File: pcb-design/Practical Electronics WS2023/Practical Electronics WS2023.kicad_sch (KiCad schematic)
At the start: 38 parts, among them IC1 SN74LVC2G04DBVT, J1 PWR Jack, J2 MIDI Input, J3 MIDI Thru out, J4 Conn_01x03, J5 ISP, Q1 Q_NMOS_DGS, SW1 SW_SPDT, SW2 SW_SPDT, SW4 SW_SPDT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

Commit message: removed led detector
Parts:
- removed Q1: Q_NMOS_DGS, symbol Device:Q_NMOS_DGS
- removed R8: 10k, symbol Device:R
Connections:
- net LED GND is gone; now on net GND: J4.1 (Pin_1)
- no-connect marks 22 -> 23
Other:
- note removed: "LED strip detector"
- note removed: "When LED is connected - PIN3 is LOW. Internal pull-up resistor should be used."
- moved on the sheet: J4

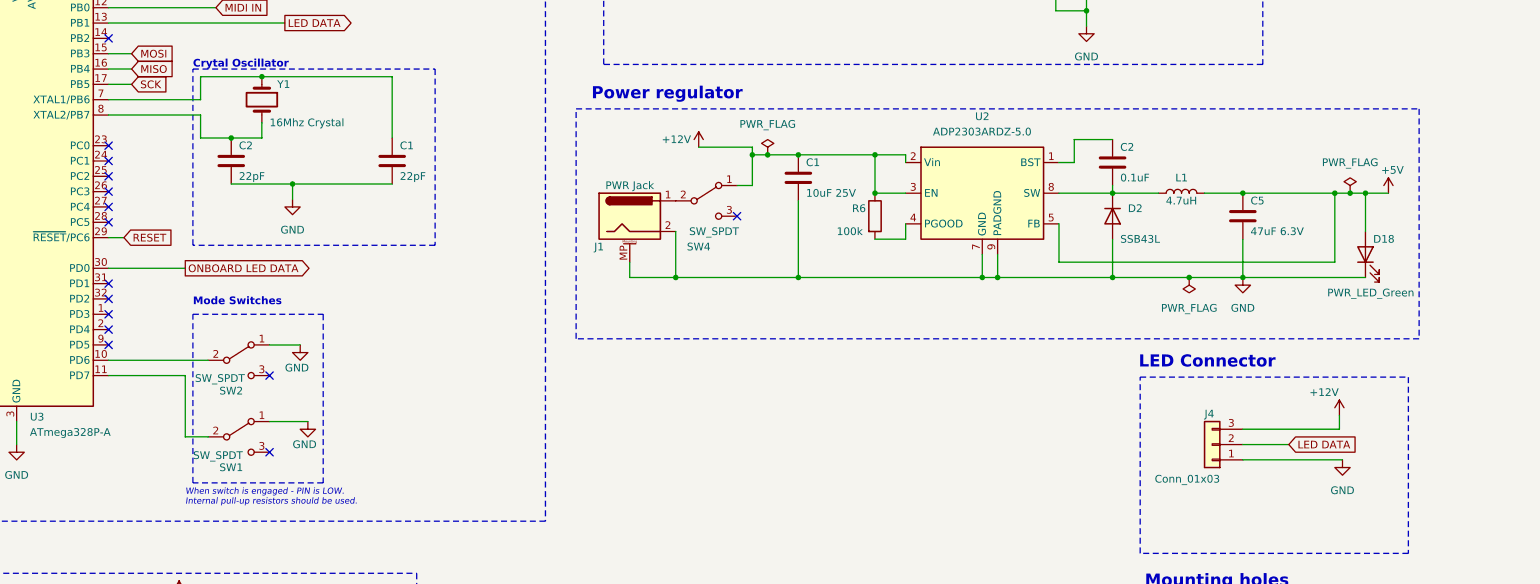
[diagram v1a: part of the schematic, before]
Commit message: replaced sitches with switch connectors
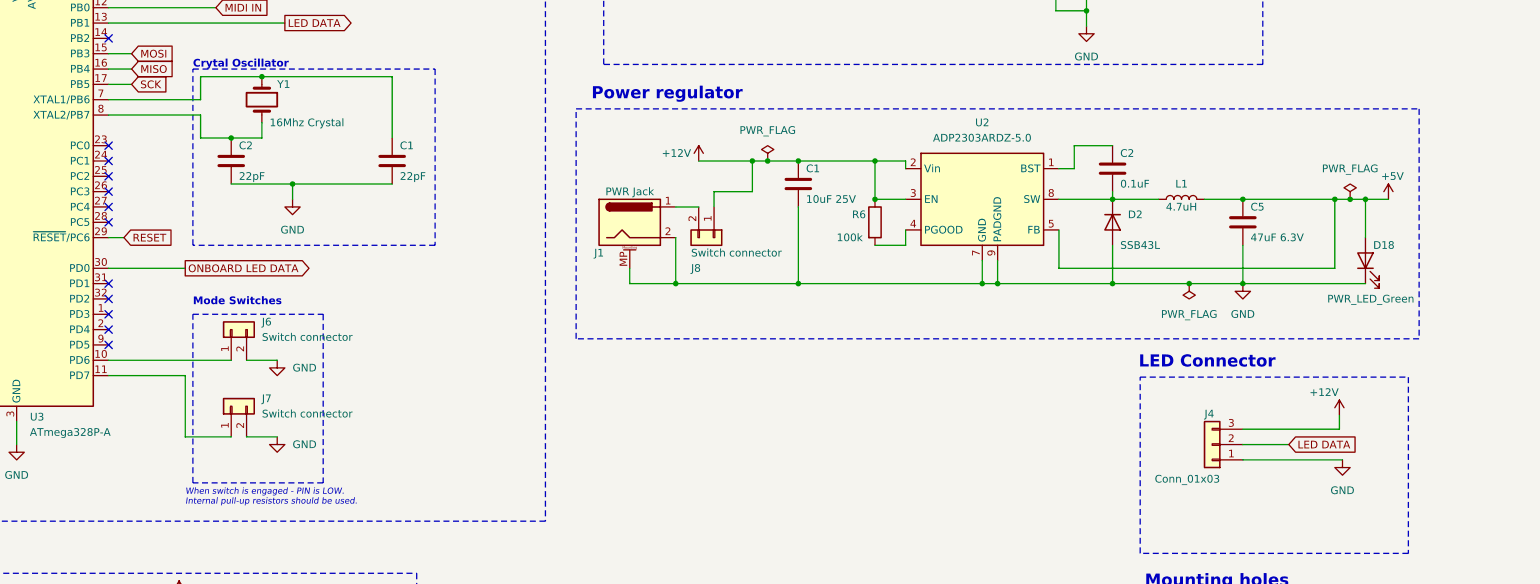
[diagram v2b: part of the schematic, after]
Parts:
- removed SW1, SW2, SW4: SW_SPDT, symbol Switch:SW_SPDT
- added J6, J7, J8: Switch connector, symbol Connector_Generic:Conn_01x02
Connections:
- net +12V: now also J8.1 (Pin_1)
- net GND: now also J6.2 (Pin_2), J7.2 (Pin_2)
- net at U3.10 (PD6): now also J6.1 (Pin_1)
- net at J1.1: now also J8.2 (Pin_2)
- net at U3.11 (PD7): now also J7.1 (Pin_1)
- no-connect marks 23 -> 20
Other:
- moved on the sheet: C1, C2, C5, D18, D2, J1, L1, R6, U2

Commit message: most of the footprints assigned
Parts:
- C1: footprint (none) -> Capacitor_SMD:C_Elec_4x5.4
- C1, C2, C5: footprint (none) -> Capacitor_SMD:C_1206_3216Metric_Pad1.33x1.80mm_HandSolder
- D18: footprint (none) -> LED_SMD:LED_1206_3216Metric
- H1, H2, H3, H4: footprint (none) -> MountingHole:MountingHole_3mm
- J1: footprint (none) -> Connector_BarrelJack:BarrelJack_Horizontal
- J4: footprint (none) -> Connector_JST:JST_PH_B3B-PH-K_1x03_P2.00mm_Vertical
- J5: footprint (none) -> Connector_PinHeader_2.00mm:PinHeader_2x03_P2.00mm_Vertical
- J6, J7, J8: footprint (none) -> Connector_JST:JST_PH_B2B-PH-K_1x02_P2.00mm_Vertical
- L1, R2, R3, R4, R5, R6, R7: footprint (none) -> Resistor_SMD:R_1206_3216Metric_Pad1.30x1.75mm_HandSolder
- U1: footprint (none) -> Package_DIP:SMDIP-8_W9.53mm
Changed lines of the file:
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@@
       (effects (font (size 1.27 1.27)))
     )
-    (property "Footprint" "" (at 85.344 145.034 90)
+    (property "Footprint" "Resistor_SMD:R_1206_3216Metric_Pad1.30x1.75mm_HandSolder" (at 85.344 145.034 90)
       (effects (font (size 1.27 1.27)) hide)
     )
@@
       (effects (font (size 1.27 1.27)) (justify left))
     )
-    (property "Footprint" "" (at 180.0352 76.2 0)
+    (property "Footprint" "Capacitor_SMD:C_Elec_4x5.4" (at 180.0352 76.2 0)
       (effects (font (size 1.27 1.27)) hide)
     )
@@
       (effects (font (size 1.27 1.27)) (justify left))
     )
-    (property "Footprint" "" (at 231.902 28.448 0)
+    (property "Footprint" "Resistor_SMD:R_1206_3216Metric_Pad1.30x1.75mm_HandSolder" (at 231.902 28.448 0)
       (effects (font (size 1.27 1.27)) hide)
     )
@@
       (effects (font (size 1.27 1.27)))
     )
-    (property "Footprint" "" (at 218.948 37.338 0)
+    (property "Footprint" "Package_DIP:SMDIP-8_W9.53mm" (at 218.948 37.338 0)
       (effects (font (size 1.27 1.27)) hide)
     )
@@
       (effects (font (size 1.27 1.27)))
     )
-    (property "Footprint" "" (at 150.368 185.801 0)
+    (property "Footprint" "Connector_PinHeader_2.00mm:PinHeader_2x03_P2.00mm_Vertical" (at 150.368 185.801 0)
       (effects (font (size 1.27 1.27)) hide)
     )
@@
       (effects (font (size 1.27 1.27)) (justify left))
     )
-    (property "Footprint" "" (at 226.822 38.608 0)
+    (property "Footprint" "Resistor_SMD:R_1206_3216Metric_Pad1.30x1.75mm_HandSolder" (at 226.822 38.608 0)
       (effects (font (size 1.27 1.27)) hide)
     )
@@
       (effects (font (size 1.27 1.27)) (justify left))
     )
-    (property "Footprint" "" (at 189.992 78.74 90)
+    (property "Footprint" "Resistor_SMD:R_1206_3216Metric_Pad1.30x1.75mm_HandSolder" (at 189.992 78.74 90)
       (effects (font (size 1.27 1.27)) hide)
     )
@@
       (effects (font (size 1.27 1.27)) (justify left))
     )
-    (property "Footprint" "" (at 262.128 145.669 0)
+    (property "Footprint" "MountingHole:MountingHole_3mm" (at 262.128 145.669 0)
       (effects (font (size 1.27 1.27)) hide)
     )
@@
       (effects (font (size 1.27 1.27)) (justify right))
     )
-    (property "Footprint" "" (at 75.4888 161.036 0)
+    (property "Footprint" "Capacitor_SMD:C_1206_3216Metric_Pad1.33x1.80mm_HandSolder" (at 75.4888 161.036 0)
       (effects (font (size 1.27 1.27)) hide)
     )
@@
       (effects (font (size 1.27 1.27)) (justify left))
     )
-    (property "Footprint" "" (at 240.919 156.718 0)
+    (property "Footprint" "MountingHole:MountingHole_3mm" (at 240.919 156.718 0)
       (effects (font (size 1.27 1.27)) hide)
     )
@@
       (effects (font (size 1.27 1.27)))
     )
-    (property "Footprint" "" (at 242.57 74.93 0)
+    (property "Footprint" "Resistor_SMD:R_1206_3216Metric_Pad1.30x1.75mm_HandSolder" (at 242.57 74.93 0)
       (effects (font (size 1.27 1.27)) hide)
     )
@@
       (effects (font (size 1.27 1.27)))
     )
-    (property "Footprint" "" (at 86.614 160.274 90)
+    (property "Footprint" "Resistor_SMD:R_1206_3216Metric_Pad1.30x1.75mm_HandSolder" (at 86.614 160.274 90)
       (effects (font (size 1.27 1.27)) hide)
     )
@@
       (effects (font (size 1.27 1.27)) (justify right))
     )
-    (property "Footprint" "" (at 85.09 96.52 0)
+    (property "Footprint" "Connector_JST:JST_PH_B2B-PH-K_1x02_P2.00mm_Vertical" (at 85.09 96.52 0)
       (effects (font (size 1.27 1.27)) hide)
     )
@@
       (effects (font (size 1.27 1.27)) (justify right))
     )
-    (property "Footprint" "" (at 85.09 109.22 0)
+    (property "Footprint" "Connector_JST:JST_PH_B2B-PH-K_1x02_P2.00mm_Vertical" (at 85.09 109.22 0)
       (effects (font (size 1.27 1.27)) hide)
     )
@@
       (effects (font (size 1.27 1.27)))
     )
-    (property "Footprint" "" (at 152.4 79.756 0)
+    (property "Footprint" "Connector_BarrelJack:BarrelJack_Horizontal" (at 152.4 79.756 0)
       (effects (font (size 1.27 1.27)) hide)
     )
@@
       (effects (font (size 1.27 1.27)) (justify left))
     )
-    (property "Footprint" "" (at 22.3012 33.02 0)
+    (property "Footprint" "Capacitor_SMD:C_1206_3216Metric_Pad1.33x1.80mm_HandSolder" (at 22.3012 33.02 0)
       (effects (font (size 1.27 1.27)) hide)
     )
@@
       (effects (font (size 1.27 1.27)) (justify left))
     )
-    (property "Footprint" "" (at 262.128 157.226 0)
+    (property "Footprint" "MountingHole:MountingHole_3mm" (at 262.128 157.226 0)
       (effects (font (size 1.27 1.27)) hide)
     )
@@
       (effects (font (size 1.27 1.27)) (justify left))
     )
-    (property "Footprint" "" (at 40.5892 33.02 0)
+    (property "Footprint" "Capacitor_SMD:C_1206_3216Metric_Pad1.33x1.80mm_HandSolder" (at 40.5892 33.02 0)
       (effects (font (size 1.27 1.27)) hide)
     )
@@
       (effects (font (size 1.27 1.27)) (justify left))
     )
-    (property "Footprint" "" (at 86.0552 72.39 0)
+    (property "Footprint" "Capacitor_SMD:C_1206_3216Metric_Pad1.33x1.80mm_HandSolder" (at 86.0552 72.39 0)
       (effects (font (size 1.27 1.27)) hide)
     )
@@
       (effects (font (size 1.27 1.27)) (justify left))
     )
-    (property "Footprint" "" (at 253.6952 82.55 0)
+    (property "Footprint" "Capacitor_SMD:C_1206_3216Metric_Pad1.33x1.80mm_HandSolder" (at 253.6952 82.55 0)
       (effects (font (size 1.27 1.27)) hide)
     )
@@
       (effects (font (size 1.27 1.27)) (justify right))
     )
-    (property "Footprint" "" (at 247.65 115.57 0)
+    (property "Footprint" "Connector_JST:JST_PH_B3B-PH-K_1x03_P2.00mm_Vertical" (at 247.65 115.57 0)
       (effects (font (size 1.27 1.27)) hide)
     )
@@
       (effects (font (size 1.27 1.27)) (justify right))
     )
-    (property "Footprint" "" (at 273.05 85.09 0)
+    (property "Footprint" "LED_SMD:LED_1206_3216Metric" (at 273.05 85.09 0)
       (effects (font (size 1.27 1.27)) hide)
     )
@@
       (effects (font (size 1.27 1.27)) (justify left))
     )
-    (property "Footprint" "" (at 241.046 145.542 0)
+    (property "Footprint" "MountingHole:MountingHole_3mm" (at 241.046 145.542 0)
       (effects (font (size 1.27 1.27)) hide)
     )
@@
       (effects (font (size 1.27 1.27)) (justify left))
     )
-    (property "Footprint" "" (at 232.1052 73.66 0)
+    (property "Footprint" "Capacitor_SMD:C_1206_3216Metric_Pad1.33x1.80mm_HandSolder" (at 232.1052 73.66 0)
       (effects (font (size 1.27 1.27)) hide)
     )
@@
       (effects (font (size 1.27 1.27)) (justify left))
     )
-    (property "Footprint" "" (at 31.6992 33.02 0)
+    (property "Footprint" "Capacitor_SMD:C_1206_3216Metric_Pad1.33x1.80mm_HandSolder" (at 31.6992 33.02 0)
       (effects (font (size 1.27 1.27)) hide)
     )
@@
       (effects (font (size 1.27 1.27)))
     )
-    (property "Footprint" "" (at 183.642 24.638 0)
+    (property "Footprint" "Resistor_SMD:R_1206_3216Metric_Pad1.30x1.75mm_HandSolder" (at 183.642 24.638 0)
       (effects (font (size 1.27 1.27)) hide)
     )
@@
       (effects (font (size 1.27 1.27)) (justify left))
     )
-    (property "Footprint" "" (at 165.1 81.28 0)
+    (property "Footprint" "Connector_JST:JST_PH_B2B-PH-K_1x02_P2.00mm_Vertical" (at 165.1 81.28 0)
       (effects (font (size 1.27 1.27)) hide)
     )
@@
       (effects (font (size 1.27 1.27)) (justify right))
     )
-    (property "Footprint" "" (at 110.7948 64.77 0)
-      (effects (font (size 1.27 1.27)) hide)
-    )
+    (property "Footprint" "Capacitor_SMD:C_1206_3216Metric_Pad1.33x1.80mm_HandSolder" (at 110.7948 64.77 0)
+      (effects (font (size 1.27 1.27)) hide)
+    )
